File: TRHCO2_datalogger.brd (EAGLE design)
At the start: 57.2 x 50.8 mm, 64 parts, among them J3 MicroUSB (5V), T2 MMUN2133LT1G, U1 ATMEGA328P-MU, U2 FT231XQ-R, U3 DS3234, U4 TPS61090RSAR, U5 MCP73871, U6 K30-CO2-I2C, U7 SHT31/35, U8 MCP1703/3.3V, Y2 SPARKFUN_RESONATORSMD

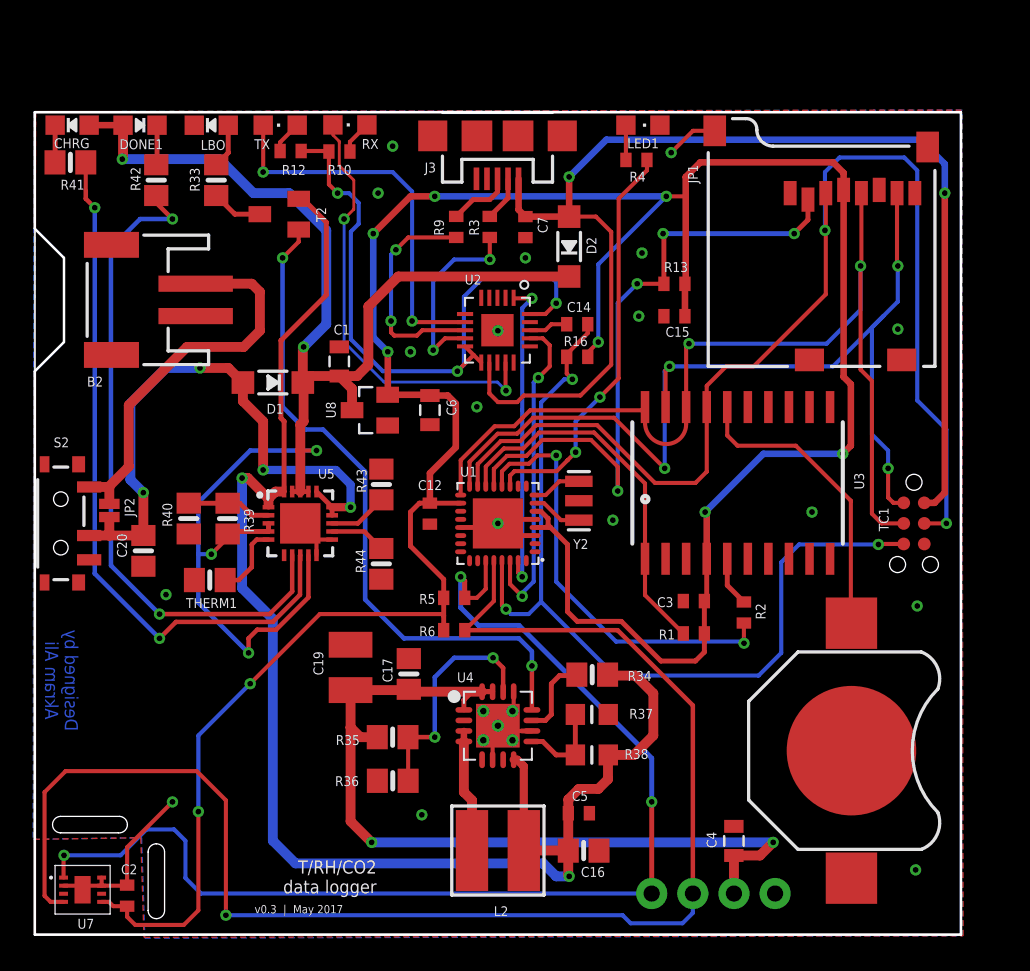
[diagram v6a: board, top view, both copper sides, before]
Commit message: Added power plane
Adjusted traces, added power planes, some other minor trace adjustments
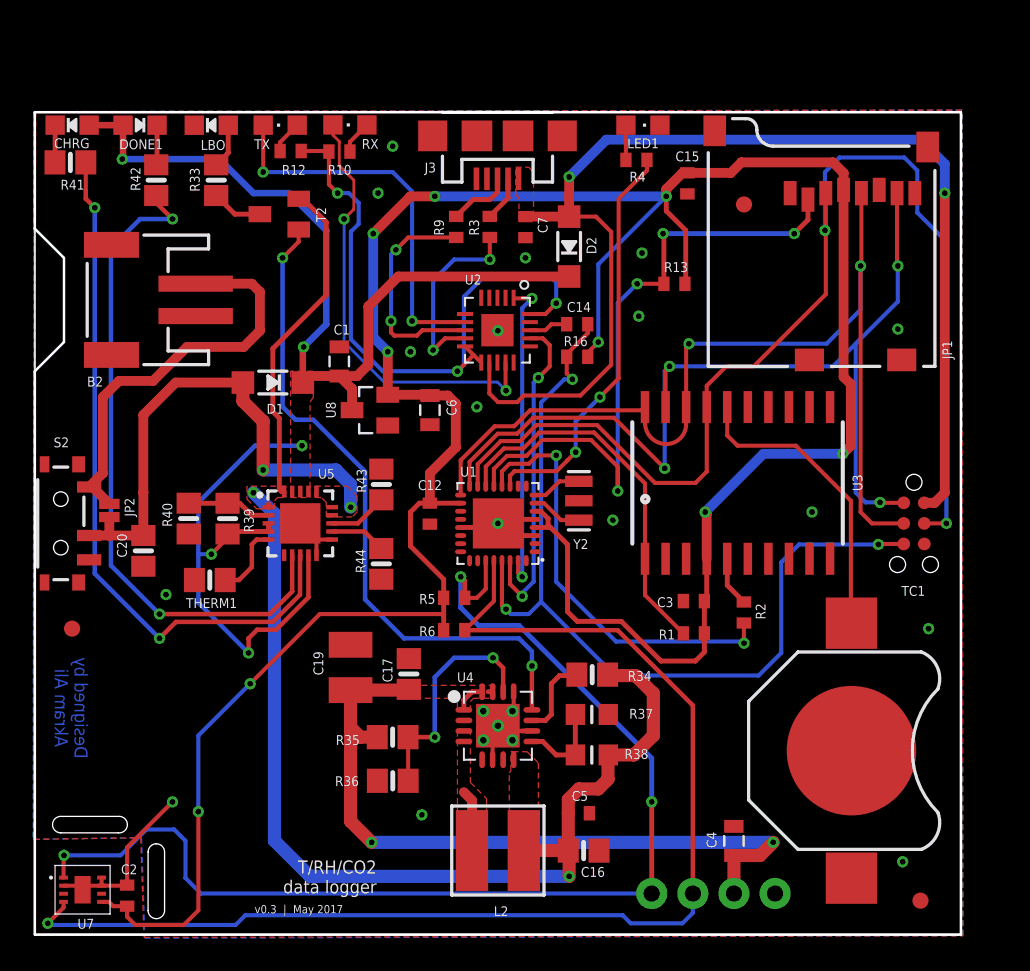
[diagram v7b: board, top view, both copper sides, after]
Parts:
- added U$1, U$2, U$3: FIDUCIAL, adafruit:FIDUCIAL_1MM
- moved C15 8.24 mm to (40.3, 46.4), turned to 270 degrees
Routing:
- net SCL: track 90.5 -> 76.2 mm
- net VBAT: track 94.9 -> 84.7 mm
- net VBUS: track 94.4 -> 84.8 mm
- net VLIPO: track 37.3 -> 32.0 mm, vias 4 -> 2
- net 5.0V: track 52.6 -> 47.8 mm
- net N$6: track 7.59 -> 3.81 mm
- net GND: track 30.7 -> 27.4 mm, vias 18 -> 17
- net USB_PWR: track 76.1 -> 73.6 mm
- net VCC: track 175.3 -> 173.4 mm
- net VLIPO_SWITCH: track 24.4 -> 25.6 mm
- added copper zone on layer 1, net 5.0V
- added copper zone on layer 1, net N$6
- added copper zone on layer 1, net USB_PWR
- added copper zone on layer 1, net VBAT
- added copper zone on layer 1, net VBUS
- added copper zone on layer 1, net VLIPO
